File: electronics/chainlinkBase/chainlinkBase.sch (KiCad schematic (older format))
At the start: 50 parts, among them J101 Power In, J102 RELAY, J103 Power In, J104 RS485, J105 RS485, J106 Logic Power Out, J107 UART, J108 Output, J109 Output, J110 Output, J111 Conn_01x06_Male, J112 Conn_01x06_Male, SW101 SW_DIP_x04, U101 AP7361C-33E, U102 TPL7407L, U103 Buck, U104 TTGO_TDisplay, U105 MCP23017_SS, U106 SN74LV1T34DBV, U107 SP485, U108 SN74LV1T34DBV

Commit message: Chainlink Base - Digikey part numbers, schematic cleanup, minor pcb tweaks
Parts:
- added TP101, TP102, TP103: TestPoint_Small, TestPoint:TestPoint_THTPad_D2.0mm_Drill1.0mm, symbol Connector:TestPoint_Small
- C102, C103: DK# (none) -> 1276-1244-1-ND
- C105, C106, C107, C108, C109, C110, C111, C112, C113, C114: DK# (none) -> 1276-2449-1-ND
- R101, R102: DK# (none) -> RMCF0805JT1K00CT-ND
- R103: value 10k -> 15k; DK# (none) -> RMCF0805JT15K0CT-ND
- U107: DK# (none) -> 1016-1171-5-ND
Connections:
- net at U104.21 (GPIO38): now also TP101.1
- net at U104.7 (GPIO15): now also TP102.1
- net at U104.9 (GPIO12): now also TP103.1
- no-connect marks 11 -> 5
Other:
- moved on the sheet: C107, C108, C109, C110, C111, C112, C113, C114, D101, D102, D103, D104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

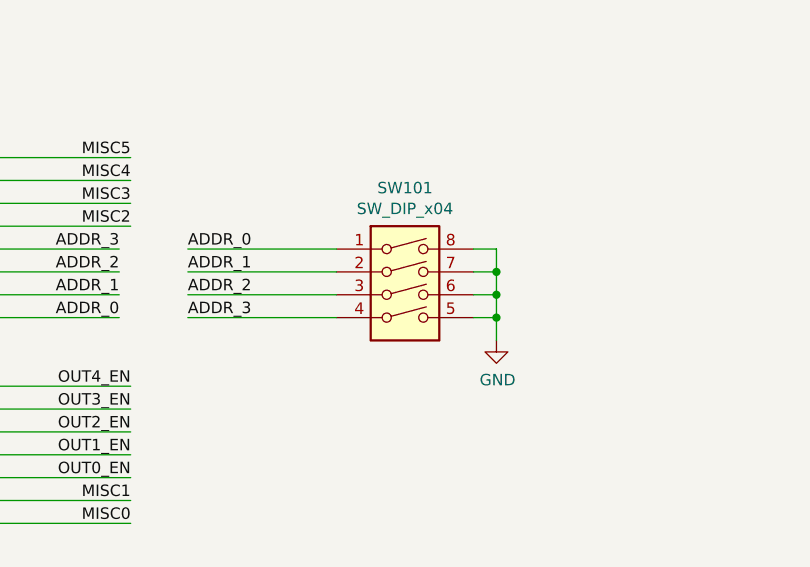
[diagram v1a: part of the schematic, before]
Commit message: Layout tweaks
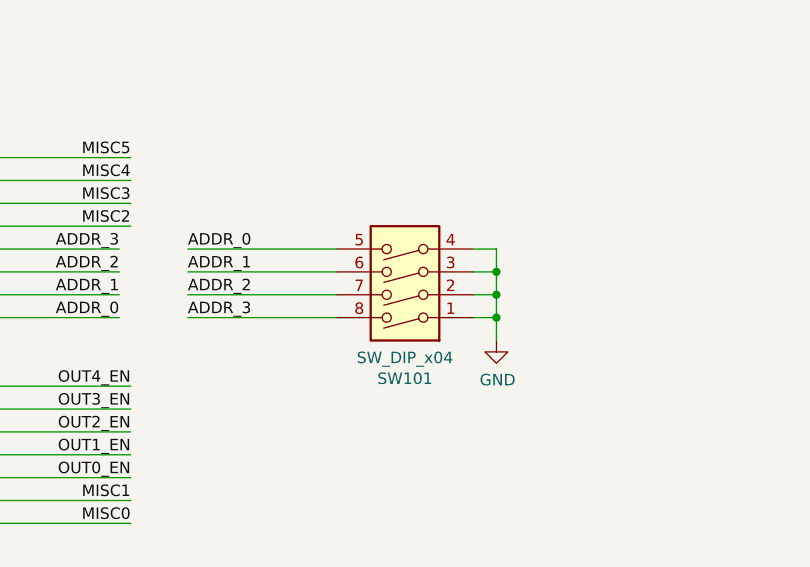
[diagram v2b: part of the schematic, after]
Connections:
- net ADDR_0: now also SW101.5; no longer SW101.1
- net ADDR_1: now also SW101.6; no longer SW101.2
- net ADDR_2: now also SW101.7; no longer SW101.3
- net ADDR_3: now also SW101.8; no longer SW101.4
- net GND: now also SW101.1, SW101.2, SW101.3, SW101.4; no longer SW101.5, SW101.6, SW101.7, SW101.8
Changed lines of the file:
@@
 L Switch:SW_DIP_x04 SW101
 U 1 1 60FDD1A2
-P 9500 4000
-F 0 "SW101" H 9500 4467 50  0000 C CNN
-F 1 "SW_DIP_x04" H 9500 4376 50  0000 C CNN
-F 2 "Button_Switch_SMD:SW_DIP_SPSTx04_Slide_Omron_A6S-410x_W8.9mm_P2.54mm" H 9500 4000 50  0001 C CNN
-F 3 "~" H 9500 4000 50  0001 C CNN
-F 4 "CT2194LPST-ND" H 9500 4000 50  0001 C CNN "DK#"
-	1    9500 4000
-	1    0    0    -1
+P 9500 3900
+F 0 "SW101" H 9500 4367 50  0000 C CNN
+F 1 "SW_DIP_x04" H 9500 4276 50  0000 C CNN
+F 2 "Button_Switch_SMD:SW_DIP_SPSTx04_Slide_Omron_A6S-410x_W8.9mm_P2.54mm" H 9500 3900 50  0001 C CNN
+F 3 "~" H 9500 3900 50  0001 C CNN
+F 4 "CT2194LPST-ND" H 9500 3900 50  0001 C CNN "DK#"
+	1    9500 3900
+	-1   0    0    1
 $EndComp
 Text Notes 6100 5250 0    50   ~ 0

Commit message: Updates
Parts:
- JP101: footprint Connector_PinHeader_2.54mm:PinHeader_1x02_P2.54mm_Vertical -> Connector_PinHeader_2.54mm:PinHeader_1x03_P2.54mm_Vertical; symbol Device:Jumper_NO_Small -> Jumper:Jumper_3_Bridged12
- U103: footprint Buck:BuckModule -> Buck:BuckModuleBackSilk
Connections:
- no-connect marks 5 -> 6
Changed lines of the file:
@@
 F 0 "U103" H 2137 2675 50  0000 C CNN
 F 1 "Buck" H 2137 2584 50  0000 C CNN
-F 2 "Buck:BuckModule" H 2100 2350 50  0001 C CNN
+F 2 "Buck:BuckModuleBackSilk" H 2100 2350 50  0001 C CNN
 F 3 "" H 2100 2350 50  0001 C CNN
 	1    2100 2350
@@
 L power:GND #PWR0141
 U 1 1 608A06A5
-P 15400 8650
-F 0 "#PWR0141" H 15400 8400 50  0001 C CNN
-F 1 "GND" H 15405 8477 50  0000 C CNN
-F 2 "" H 15400 8650 50  0001 C CNN
-F 3 "" H 15400 8650 50  0001 C CNN
-	1    15400 8650
-	1    0    0    -1
-$EndComp
-$Comp
-L Device:Jumper_NO_Small JP101
+P 15000 8800
+F 0 "#PWR0141" H 15000 8550 50  0001 C CNN
+F 1 "GND" H 15005 8627 50  0000 C CNN
+F 2 "" H 15000 8800 50  0001 C CNN
+F 3 "" H 15000 8800 50  0001 C CNN
+	1    15000 8800
+	1    0    0    -1
+$EndComp
+$Comp
+L Jumper:Jumper_3_Bridged12 JP101
 U 1 1 608A0DD3
-P 14850 8550
-F 0 "JP101" H 14850 8735 50  0000 C CNN
-F 1 "LEDs" H 14850 8644 50  0000 C CNN
-F 2 "Connector_PinHeader_2.54mm:PinHeader_1x02_P2.54mm_Vertical" H 14850 8550 50  0001 C CNN
-F 3 "~" H 14850 8550 50  0001 C CNN
-	1    14850 8550
+P 15000 8550
+F 0 "JP101" H 15000 8735 50  0000 C CNN
+F 1 "LEDs" H 15000 8644 50  0000 C CNN
+F 2 "Connector_PinHeader_2.54mm:PinHeader_1x03_P2.54mm_Vertical" H 15000 8550 50  0001 C CNN
+F 3 "~" H 15000 8550 50  0001 C CNN
+	1    15000 8550
 	1    0    0    -1
 $EndComp
@@
 	14050 8550 14750 8550
 Wire Wire Line
-	14950 8550 15400 8550
-Wire Wire Line
-	15400 8550 15400 8650
+	15000 8700 15000 8800
 $Comp
 L power:GND #PWR0142
@@
 Wire Notes Line
 	12350 500  12350 9250
+NoConn ~ 15250 8550
 $EndSCHEMATC

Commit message: Add pull-down for load switches, move LED jumpers and make solder-bridgeable
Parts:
- JP101: footprint Connector_PinHeader_2.54mm:PinHeader_1x03_P2.54mm_Vertical -> ModifiedSymbols:PinHeader_1x03_P2.54mm_Vertical_SolderJumper
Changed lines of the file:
@@
 F 0 "JP101" H 15000 8735 50  0000 C CNN
 F 1 "LEDs" H 15000 8644 50  0000 C CNN
-F 2 "Connector_PinHeader_2.54mm:PinHeader_1x03_P2.54mm_Vertical" H 15000 8550 50  0001 C CNN
+F 2 "ModifiedSymbols:PinHeader_1x03_P2.54mm_Vertical_SolderJumper" H 15000 8550 50  0001 C CNN
 F 3 "~" H 15000 8550 50  0001 C CNN
 	1    15000 8550

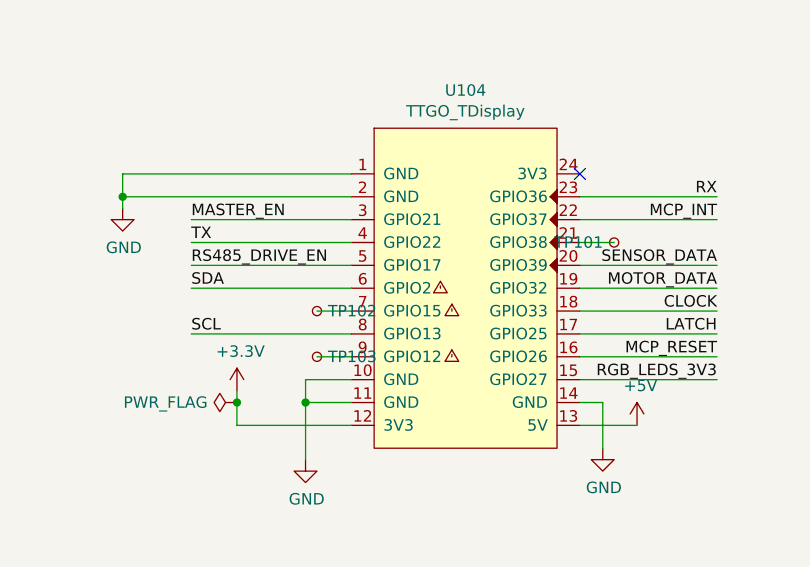
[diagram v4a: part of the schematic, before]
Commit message: Update Chainlink Base electronics to fix pinout mixup (#183)
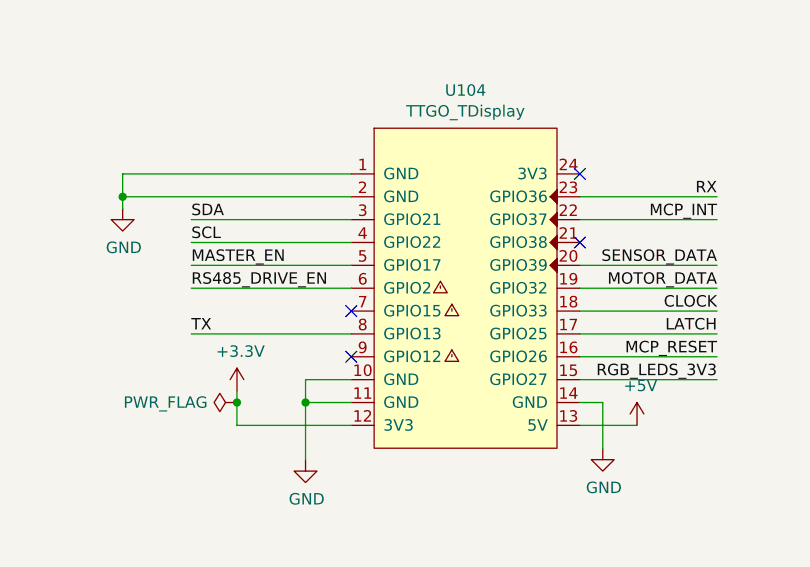
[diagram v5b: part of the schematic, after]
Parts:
- removed TP101, TP102, TP103: TestPoint_Small, TestPoint:TestPoint_THTPad_D2.0mm_Drill1.0mm, symbol Connector:TestPoint_Small
- U104: footprint ESP32:T-DISPLAY -> ESP32:T-DISPLAY_extra_pins
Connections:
- net MASTER_EN: now also U104.5 (GPIO17); no longer U104.3 (GPIO21)
- net RS485_DRIVE_EN: now also U104.6 (GPIO2); no longer U104.5 (GPIO17)
- net SCL: now also U104.4 (GPIO22); no longer U104.8 (GPIO13)
- net SDA: now also U104.3 (GPIO21); no longer U104.6 (GPIO2)
- net TX: now also U104.8 (GPIO13); no longer U104.4 (GPIO22)
- no-connect marks 6 -> 9
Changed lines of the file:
@@
-	1    0    0    -1
-$EndComp
-$Comp
-L power:+3.3V #PWR0115
-U 1 1 60E226B9
-P 5000 2700
-F 0 "#PWR0115" H 5000 2550 50  0001 C CNN
-F 1 "+3.3V" H 5015 2873 50  0000 C CNN
-F 2 "" H 5000 2700 50  0001 C CNN
-F 3 "" H 5000 2700 50  0001 C CNN
-	1    5000 2700
 	1    0    0    -1
 $EndComp
@@
 	4850 2800 4850 2700
 Wire Wire Line
-	4850 2700 5000 2700
-Wire Wire Line
-	5000 2700 5150 2700
-Wire Wire Line
 	5150 2700 5150 2800
-Connection ~ 5000 2700
 Wire Wire Line
 	4850 3000 4850 3100
@@
 F 0 "U104" H 2850 5015 50  0000 C CNN
 F 1 "TTGO_TDisplay" H 2850 4924 50  0000 C CNN
-F 2 "ESP32:T-DISPLAY" H 2650 4200 50  0001 C CNN
+F 2 "ESP32:T-DISPLAY_extra_pins" H 2650 4200 50  0001 C CNN
 F 3 "" H 2650 4200 50  0001 C CNN
 	1    2850 4150
@@
 Text Label 3950 4050 2    50   ~ 0
 SENSOR_DATA
-Text Label 1650 4150 0    50   ~ 0
+Text Label 1650 3850 0    50   ~ 0
 SDA
-Text Label 1650 4350 0    50   ~ 0
+Text Label 1650 3950 0    50   ~ 0
 SCL
 Text Label 3950 3750 2    50   ~ 0
 RX
-Text Label 1650 3950 0    50   ~ 0
+Text Label 1650 4350 0    50   ~ 0
 TX
 Wire Wire Line
@@
 Wire Wire Line
 	1850 4750 2350 4750
-Text Label 1650 4050 0    50   ~ 0
+Text Label 1650 4150 0    50   ~ 0
 RS485_DRIVE_EN
 Wire Wire Line
-	1650 4050 2350 4050
+	1650 4150 2350 4150
 $Comp
 L power:+3.3V #PWR0122
@@
 Connection ~ 3700 7250
 Wire Wire Line
+	1650 4350 2350 4350
+Wire Wire Line
+	1650 3850 2350 3850
+Wire Wire Line
 	1650 3950 2350 3950
-Wire Wire Line
-	1650 4150 2350 4150
-Wire Wire Line
-	1650 4350 2350 4350
 $Comp
 L power:GND #PWR0114
@@
 	9750 1350 9750 1250
 Wire Wire Line
-	2350 3850 1650 3850
-Text Label 1650 3850 0    50   ~ 0
+	2350 4050 1650 4050
+Text Label 1650 4050 0    50   ~ 0
 MASTER_EN
 Wire Wire Line
@@
 Wire Wire Line
 	1850 4650 1850 4750
-NoConn ~ 3350 3650
 Wire Wire Line
 	1000 7450 1750 7450
@@
 Wire Wire Line
 	1750 7450 3750 7450
-$Comp
-L Connector:TestPoint_Small TP102
-U 1 1 6071DE1E
-P 2200 4250
-F 0 "TP102" H 2248 4250 50  0000 L CNN
-F 1 "TestPoint_Small" H 2248 4205 50  0001 L CNN
-F 2 "TestPoint:TestPoint_THTPad_D2.0mm_Drill1.0mm" H 2400 4250 50  0001 C CNN
-F 3 "~" H 2400 4250 50  0001 C CNN
-	1    2200 4250
-	1    0    0    -1
-$EndComp
-Wire Wire Line
-	2200 4250 2350 4250
-$Comp
-L Connector:TestPoint_Small TP103
-U 1 1 60736F00
-P 2200 4450
-F 0 "TP103" H 2248 4450 50  0000 L CNN
-F 1 "TestPoint_Small" H 2248 4405 50  0001 L CNN
-F 2 "TestPoint:TestPoint_THTPad_D2.0mm_Drill1.0mm" H 2400 4450 50  0001 C CNN
-F 3 "~" H 2400 4450 50  0001 C CNN
-	1    2200 4450
-	1    0    0    -1
-$EndComp
-Wire Wire Line
-	2200 4450 2350 4450
-$Comp
-L Connector:TestPoint_Small TP101
-U 1 1 6074F1E8
-P 3500 3950
-F 0 "TP101" H 3548 3950 50  0000 L CNN
-F 1 "TestPoint_Small" H 3548 3905 50  0001 L CNN
-F 2 "TestPoint:TestPoint_THTPad_D2.0mm_Drill1.0mm" H 3700 3950 50  0001 C CNN
-F 3 "~" H 3700 3950 50  0001 C CNN
-	1    3500 3950
-	-1   0    0    1
-$EndComp
-Wire Wire Line
-	3500 3950 3350 3950
 Wire Notes Line
 	12350 500  12350 9250
 NoConn ~ 15250 8550
+NoConn ~ 3350 3950
+NoConn ~ 2350 4250
+NoConn ~ 2350 4450
+Wire Wire Line
+	5000 2700 5150 2700
+Wire Wire Line
+	4850 2700 5000 2700
+Connection ~ 5000 2700
+$Comp
+L power:+3.3V #PWR0115
+U 1 1 60E226B9
+P 5000 2700
+F 0 "#PWR0115" H 5000 2550 50  0001 C CNN
+F 1 "+3.3V" H 5015 2873 50  0000 C CNN
+F 2 "" H 5000 2700 50  0001 C CNN
+F 3 "" H 5000 2700 50  0001 C CNN
+	1    5000 2700
+	1    0    0    -1
+$EndComp
+NoConn ~ 3350 3650
 $EndSCHEMATC

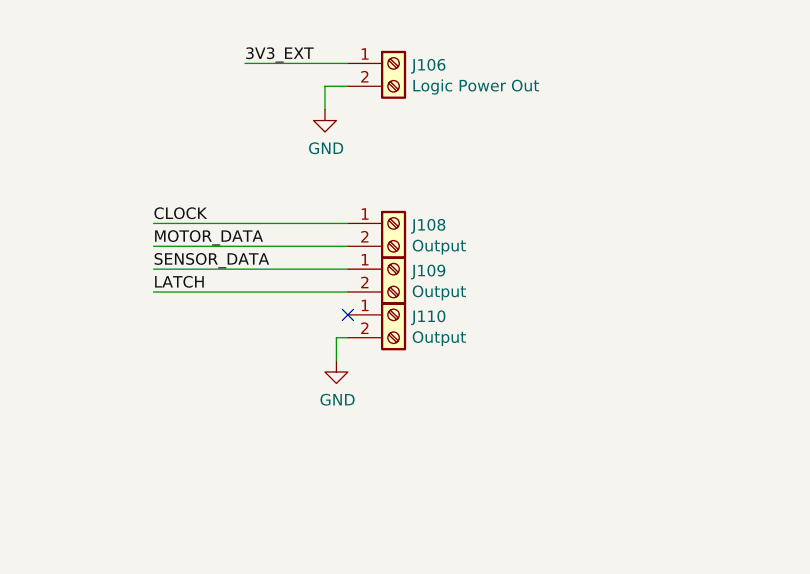
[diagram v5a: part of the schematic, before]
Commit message: Change Chainlink data connections from screw terminals to IDC (#189)
- Replace screw terminals with 2x4 IDC connectors (alternating ground) on Driver, Base, and Tester. Fixes #179
- Change Chainlink Driver Tester to all 1mm pogo pins
- Create new "Buddy" boards for connecting IDC/ribbon cable to T-Display or a breadboard
- Big readme cleanup and reorganization for clarity (hopefully!)
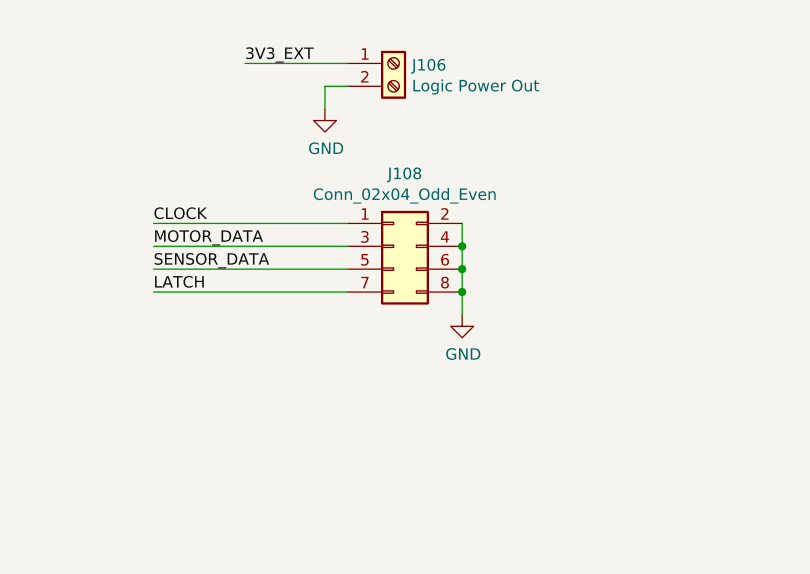
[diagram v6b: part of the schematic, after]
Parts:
- removed J108, J109, J110: Output, ScrewTerminals:Generic-5.08-2P, symbol Connector:Screw_Terminal_01x02
- added J108: Conn_02x04_Odd_Even, ModifiedSymbols:IDC-Header_2x04_P2.54mm_Vertical, symbol Connector_Generic:Conn_02x04_Odd_Even
- U104: footprint ESP32:T-DISPLAY_extra_pins -> ESP32:T-DISPLAY_extra_pins_labeled
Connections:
- net CLOCK: now also J108.1 (Pin_1)
- net GND: now also J108.2 (Pin_2), J108.4 (Pin_4), J108.6 (Pin_6), J108.8 (Pin_8)
- net LATCH: now also J108.7 (Pin_7)
- net MOTOR_DATA: now also J108.3 (Pin_3)
- net SENSOR_DATA: now also J108.5 (Pin_5)
- no-connect marks 9 -> 8
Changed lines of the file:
@@
 F 0 "U104" H 2850 5015 50  0000 C CNN
 F 1 "TTGO_TDisplay" H 2850 4924 50  0000 C CNN
-F 2 "ESP32:T-DISPLAY_extra_pins" H 2650 4200 50  0001 C CNN
+F 2 "ESP32:T-DISPLAY_extra_pins_labeled" H 2650 4200 50  0001 C CNN
 F 3 "" H 2650 4200 50  0001 C CNN
 	1    2850 4150
@@
 Wire Wire Line
 	6550 1500 6900 1500
-$Comp
-L Connector:Screw_Terminal_01x02 J108
-U 1 1 60B38901
-P 7800 7200
-F 0 "J108" H 7880 7192 50  0000 L CNN
-F 1 "Output" H 7880 7101 50  0000 L CNN
-F 2 "ScrewTerminals:Generic-5.08-2P" H 7800 7200 50  0001 C CNN
-F 3 "~" H 7800 7200 50  0001 C CNN
-F 4 "EB147A-02-D" H 7800 7200 50  0001 C CNN "DK#"
-	1    7800 7200
-	1    0    0    -1
-$EndComp
-$Comp
-L Connector:Screw_Terminal_01x02 J109
-U 1 1 60B3AC25
-P 7800 7400
-F 0 "J109" H 7880 7392 50  0000 L CNN
-F 1 "Output" H 7880 7301 50  0000 L CNN
-F 2 "ScrewTerminals:Generic-5.08-2P" H 7800 7400 50  0001 C CNN
-F 3 "~" H 7800 7400 50  0001 C CNN
-F 4 "EB147A-02-D" H 7800 7400 50  0001 C CNN "DK#"
-	1    7800 7400
-	1    0    0    -1
-$EndComp
-$Comp
-L Connector:Screw_Terminal_01x02 J110
-U 1 1 60B3B73D
-P 7800 7600
-F 0 "J110" H 7880 7592 50  0000 L CNN
-F 1 "Output" H 7880 7501 50  0000 L CNN
-F 2 "ScrewTerminals:Generic-5.08-2P" H 7800 7600 50  0001 C CNN
-F 3 "~" H 7800 7600 50  0001 C CNN
-F 4 "EB147A-02-D" H 7800 7600 50  0001 C CNN "DK#"
-	1    7800 7600
-	1    0    0    -1
-$EndComp
 Wire Wire Line
 	7600 7200 6750 7200
@@
 L power:GND #PWR0136
 U 1 1 60BA0344
-P 7550 7800
-F 0 "#PWR0136" H 7550 7550 50  0001 C CNN
-F 1 "GND" H 7555 7627 50  0000 C CNN
-F 2 "" H 7550 7800 50  0001 C CNN
-F 3 "" H 7550 7800 50  0001 C CNN
-	1    7550 7800
-	1    0    0    -1
-$EndComp
-Wire Wire Line
-	7600 7700 7550 7700
-Wire Wire Line
-	7550 7700 7550 7800
-NoConn ~ 7600 7600
+P 8100 7600
+F 0 "#PWR0136" H 8100 7350 50  0001 C CNN
+F 1 "GND" H 8105 7427 50  0000 C CNN
+F 2 "" H 8100 7600 50  0001 C CNN
+F 3 "" H 8100 7600 50  0001 C CNN
+	1    8100 7600
+	1    0    0    -1
+$EndComp
 Wire Wire Line
 	6550 1200 6900 1200
@@
 $EndComp
 NoConn ~ 3350 3650
+$Comp
+L Connector_Generic:Conn_02x04_Odd_Even J108
+U 1 1 61826671
+P 7800 7300
+F 0 "J108" H 7850 7617 50  0000 C CNN
+F 1 "Conn_02x04_Odd_Even" H 7850 7526 50  0000 C CNN
+F 2 "ModifiedSymbols:IDC-Header_2x04_P2.54mm_Vertical" H 7800 7300 50  0001 C CNN
+F 3 "~" H 7800 7300 50  0001 C CNN
+	1    7800 7300
+	1    0    0    -1
+$EndComp
+Wire Wire Line
+	8100 7600 8100 7500
+Connection ~ 8100 7300
+Wire Wire Line
+	8100 7300 8100 7200
+Connection ~ 8100 7400
+Wire Wire Line
+	8100 7400 8100 7300
+Connection ~ 8100 7500
+Wire Wire Line
+	8100 7500 8100 7400
 $EndSCHEMATC
